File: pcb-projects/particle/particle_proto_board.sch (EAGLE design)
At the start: 38 parts, among them IC1 ATTINY20-MMH, IC2 DMC2400V, IC3 DMC2400V

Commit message: routing board
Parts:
- removed SPI: 332-06, con-garry:332-06
- removed TP10, TP11, TP12, TP13, TP14, TP4, TP5, TP6, TP7, TP8, TP9: TPSPAD1-13, testpad:TPSPAD1-13
- added C1: 100n, rcl:C-EUC0805
- added ISP: 332-06, con-garry:332-06
- added PAD1, PAD4, PAD5: TP1, wirepad:1,6/0,9
- added PAD10: TP10, wirepad:1,6/0,9
- added PAD11: TP11, wirepad:1,6/0,9
- added PAD2: TP2, wirepad:1,6/0,9
- added PAD3: TP3, wirepad:1,6/0,9
- added PAD6: TP6, wirepad:1,6/0,9
- added PAD7: TP7, wirepad:1,6/0,9
- added PAD8: TP8, wirepad:1,6/0,9
- added PAD9: TP9, wirepad:1,6/0,9
- R1, R12, R2: device rcl:R-EU_R1210 -> rcl:R-EU_R0805
- R13, R14, R3, R4, R5, R6, R9: value 470 -> 1k; device rcl:R-EU_R1210 -> rcl:R-EU_R0805
- renumbered RXB1 to RXB, RXB2 to RXA, RXB_LED1 to RXB_LED, RXB_LED2 to RXA_LED, TXB1 to TXB, TXB2 to TXA, TXB_LED1 to TXB_LED, TXB_LED2 to TXA_LED
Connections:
- removed net MISO: IC1B.PB2, LED3.A, SPI-1.S, TP12.PP
- removed net PWR_TX_A: IC1B.PA4, IC2A.G, TP14.PP
- removed net RX_A: IC1B.PA5, IC2B.D, RXA.P, RXA_LED.A, TP4.PP
- removed net TPI_CLK: IC1B.PB0, TPI-3.S
- new net MISO/SW_PWR_RX_A: IC1B.PB2, IC2B.G, ISP-1.S, PAD7.P
- new net TPI_CLK/SW_PWR_RX_A: IC1B.PB0, IC2B.D, PAD6.P, RXA.P, RXA_LED.A, TPI-3.S
- new net TPI_DATA/MOSI/PWR_TX_A: IC1B.PB1, IC2A.G, PAD5.P
- net GND: now also C1.2, ISP-6.S; no longer SPI-6.S
- net N$1: now also PAD8.P; no longer TP7.PP
- net N$2: now also PAD4.P; no longer TP6.PP
- net N$21: now also PAD1.P; no longer TP10.PP
- net PWR_TX_B: now also PAD9.P; no longer TP13.PP
- net RESET: now also ISP-5.S; no longer SPI-5.S
- net RX_B: now also PAD10.P; no longer TP8.PP
- net SCK: now also ISP-3.S, PAD2.P; no longer SPI-3.S, TP11.PP
- net SW_PWR_RX_A: now also IC1B.PA5, LED3.A, PAD3.P; no longer IC1B.PA3, IC2B.G, TP5.PP
- net SW_PWR_RX_B: now also PAD11.P; no longer TP9.PP
- net TPI_DATA/MOSI: now also ISP-4.S; no longer IC1B.PB1, SPI-4.S
- net VCC: now also C1.1, ISP-2.S; no longer SPI-2.S
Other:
- note added: "RX/TX-A"
- note added: "RX/TX-B"
- moved on the sheet: IC1B, LED1, LED2, LED3, R1, R3, R4, R5, RESET-SW, TPI-1, TPI-2, TPI-3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

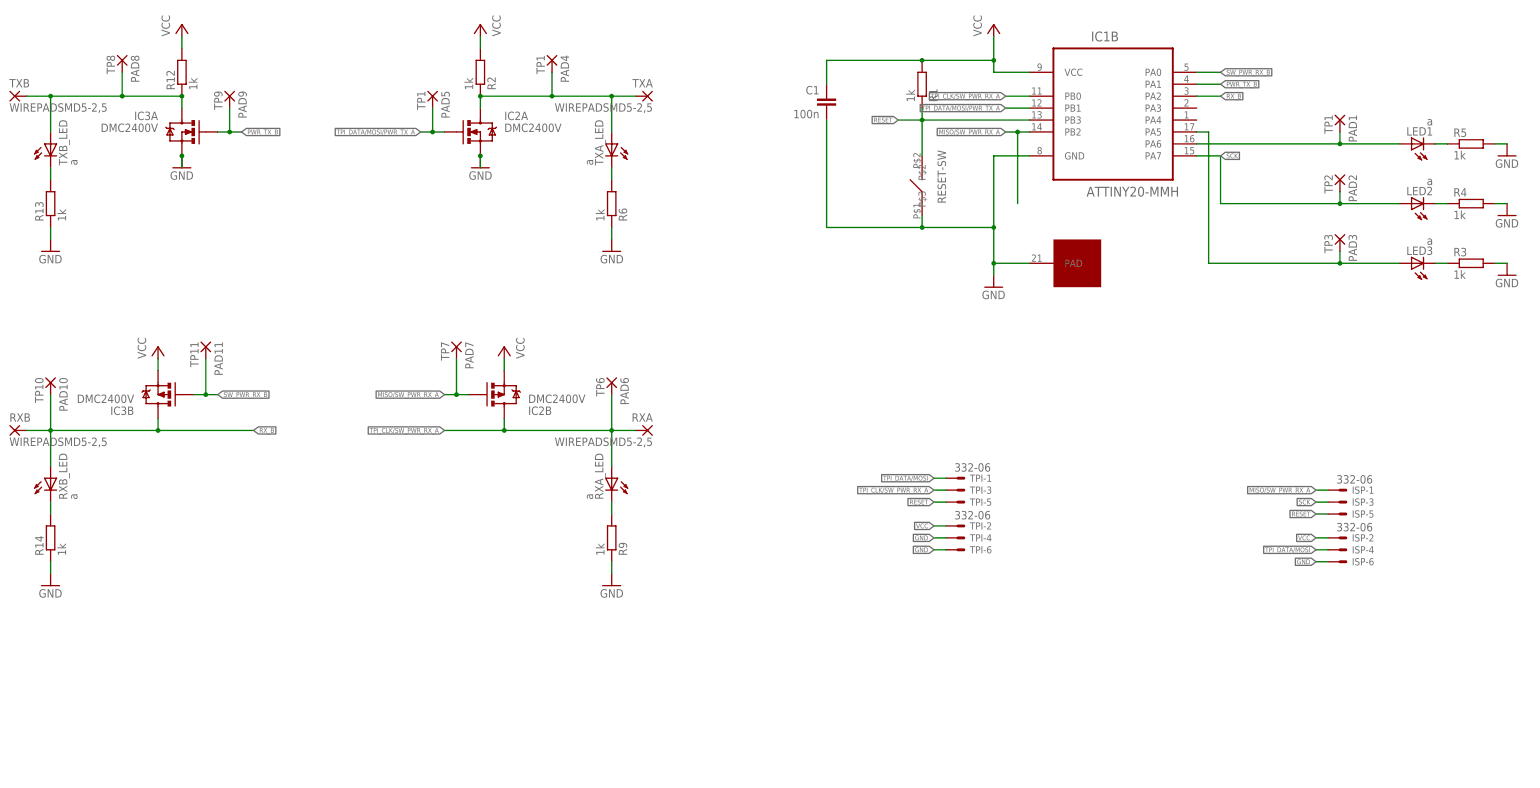
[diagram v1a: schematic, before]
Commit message: close #26, close #31, close #30, close #28, close #25, close #24, close #23
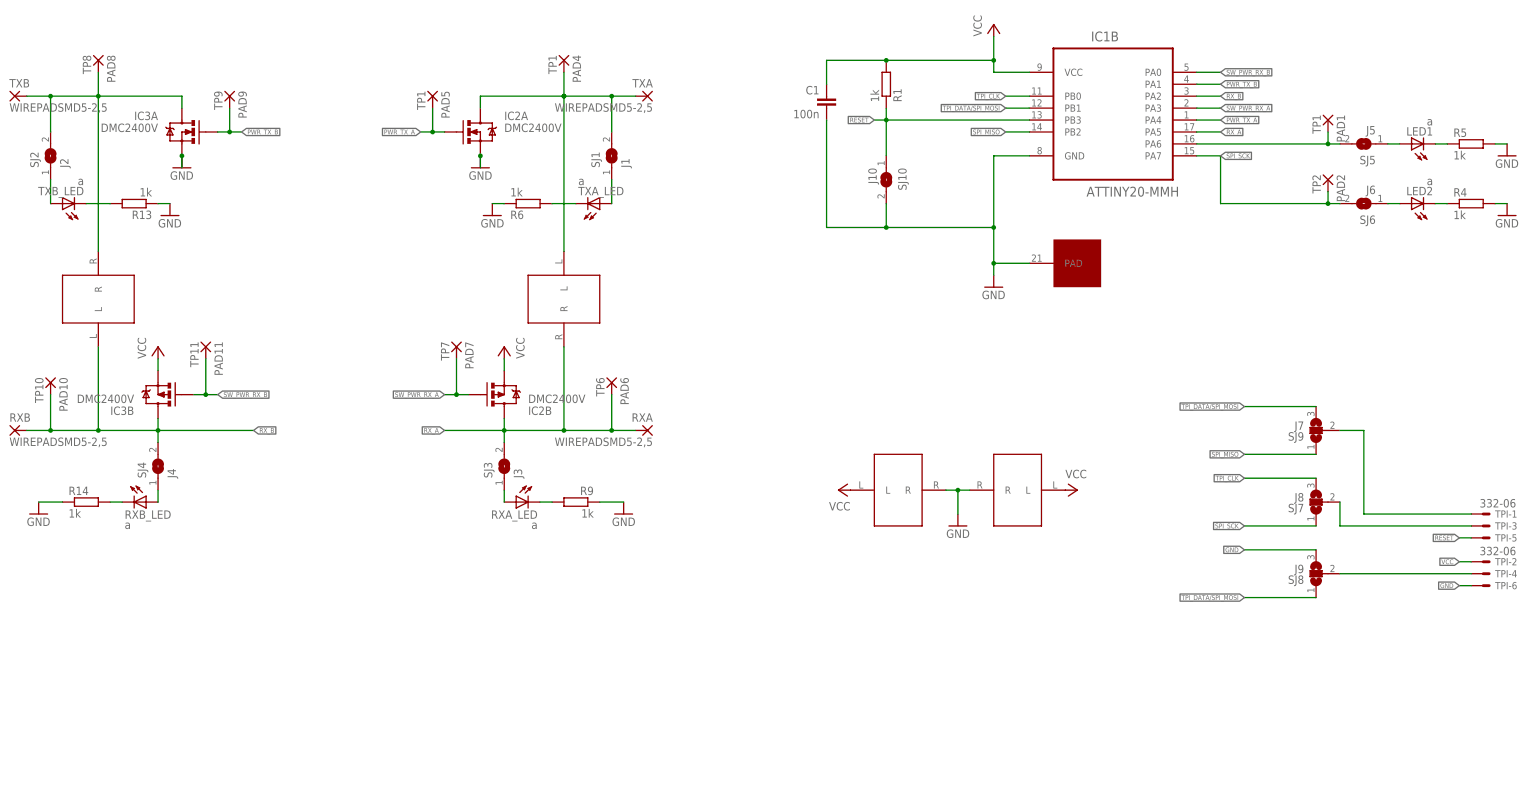
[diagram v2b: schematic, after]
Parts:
- removed ISP: 332-06, con-garry:332-06
- removed LED3: a, led:LEDSML1206
- removed PAD3: TP3, wirepad:1,6/0,9
- removed R12, R2, R3: 1k, rcl:R-EU_R0805
- removed RESET-SW: PAD-RESET-SWITCH, reset_pad:PAD-RESET-SWITCH
- added SJ1: J1, jumper:SJ
- added SJ10: J10, jumper:SJ
- added SJ2: J2, jumper:SJ
- added SJ3: J3, jumper:SJ
- added SJ4: J4, jumper:SJ
- added SJ5: J5, jumper:SJ
- added SJ6: J6, jumper:SJ
- added SJ7: J8, jumper:SJ2W
- added SJ8: J9, jumper:SJ2W
- added SJ9: J7, jumper:SJ2W
- added U$1, U$2, U$3, U$4: SMA-DUAL-CONNSMALL, connectors:SMA-DUAL-CONNSMALL
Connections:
- removed net MISO/SW_PWR_RX_A: IC1B.PB2, IC2B.G, ISP-1.S, PAD7.P
- removed net N$26: LED3.C, R3.1
- removed net SCK: IC1B.PA7, ISP-3.S, LED2.A, PAD2.P
- removed net TPI_CLK/SW_PWR_RX_A: IC1B.PB0, IC2B.D, PAD6.P, RXA.P, RXA_LED.A, TPI-3.S
- removed net TPI_DATA/MOSI: ISP-4.S, TPI-1.S
- removed net TPI_DATA/MOSI/PWR_TX_A: IC1B.PB1, IC2A.G, PAD5.P
- new net N$11: IC1B.PA6, PAD1.P, SJ5.2
- new net N$12: RXA_LED.A, SJ3.1
- new net N$13: SJ2.1, TXB_LED.A
- new net N$14: SJ1.1, TXA_LED.A
- new net N$15: SJ8.2, TPI-4.S
- new net N$17: LED2.A, SJ6.1
- new net N$18: LED1.A, SJ5.1
- new net N$20: SJ7.2, TPI-3.S
- new net N$7: RXB_LED.A, SJ4.1
- new net PWR_TX_A: IC1B.PA4, IC2A.G, PAD5.P
- new net RX_A: IC1B.PA5, IC2B.D, PAD6.P, RXA.P, SJ3.2, U$1.R
- new net SPI_MISO: IC1B.PB2, SJ9.1
- new net SPI_SCK: IC1B.PA7, PAD2.P, SJ6.2, SJ7.1
- new net TPI_CLK: IC1B.PB0, SJ7.3
- new net TPI_DATA/SPI_MOSI: IC1B.PB1, SJ8.1, SJ9.3
- net GND: now also SJ10.2, SJ8.3, U$3.R, U$4.R; no longer ISP-6.S, R3.2, RESET-SW.P$2, TPI-4.S
- net N$1: now also SJ2.2, U$2.R; no longer R12.1, TXB_LED.A
- net N$2: now also SJ1.2, U$1.L; no longer R2.1, TXA_LED.A
- net N$21: now also SJ9.2, TPI-1.S; no longer IC1B.PA6, LED1.A, PAD1.P
- net RESET: now also SJ10.1; no longer ISP-5.S, RESET-SW.P$3
- net RX_B: now also SJ4.2, U$2.L; no longer RXB_LED.A
- net SW_PWR_RX_A: now also IC1B.PA3, IC2B.G, PAD7.P; no longer IC1B.PA5, LED3.A, PAD3.P
- net VCC: now also U$3.L, U$4.L; no longer ISP-2.S, R12.2, R2.2
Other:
- note added: "POWER SUPPLY"
- note added: "TPI/SPI-HEADER"
- moved on the sheet: PAD1, PAD2, PAD4, PAD8, R1, R13, R14, R6, R9, RXA_LED, RXB_LED, TPI-1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

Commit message: close #27, close #19, close #30,skip / close #18, skip / close #14
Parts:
- removed PAD10: TP10, wirepad:1,6/0,9
- removed PAD11: TP11, wirepad:1,6/0,9
- removed PAD4, PAD5: TP1, wirepad:1,6/0,9
- removed PAD6: TP6, wirepad:1,6/0,9
- removed PAD7: TP7, wirepad:1,6/0,9
- removed PAD8: TP8, wirepad:1,6/0,9
- removed PAD9: TP9, wirepad:1,6/0,9
- removed SJ1: J1, jumper:SJ
- removed SJ2: J2, jumper:SJ
- removed SJ3: J3, jumper:SJ
- removed SJ4: J4, jumper:SJ
- removed SJ7: J8, jumper:SJ2W
- removed SJ8: J9, jumper:SJ2W
- removed SJ9: J7, jumper:SJ2W
- removed TPI: 332-06, con-garry:332-06
- removed U$1, U$2, U$3, U$4: SMA-DUAL-CONNSMALL, connectors:SMA-DUAL-CONNSMALL
- added GND_B: GND_B, wirepad:1,6/0,9
- added GND_T: GND_T, wirepad:1,6/0,9
- added PI: 332-06, con-garry:332-06
- added PWR_TX_A: PWR_TX_A, wirepad:1,6/0,9
- added PWR_TX_B: PWR_TX_B, wirepad:1,6/0,9
- added SW1: SW1, jumper:SJ2W
- added SW2: SW2, jumper:SJ2W
- added SW3: SW3, jumper:SJ2W
- added SWLED3: J2, jumper:SJ
- added SWLED4: J4, jumper:SJ
- added SWLED5: J1, jumper:SJ
- added SWLED6: J3, jumper:SJ
- added SW_PWR_RX_A: SW_PWR_RX_A, wirepad:1,6/0,9
- added SW_PWR_RX_B: SW_PWR_RX_B, wirepad:1,6/0,9
- added TPRXA: TPRXA, wirepad:1,6/0,9
- added TPRXB: TPRXB, wirepad:1,6/0,9
- added TPTXA: TPTXA, wirepad:1,6/0,9
- added TPTXB: TPTXB, wirepad:1,6/0,9
- added VCC_B: VCC_B, wirepad:1,6/0,9
- added VCC_T: VCC_T, wirepad:1,6/0,9
- LED1, LED2, RXA_LED, RXB_LED, TXA_LED, TXB_LED: value a -> x
- RESET: value J10 -> RESET
- RXA: value WIREPADSMD5-2,5 -> RXA; device wirepad:WIREPADSMD5-2,5 -> wirepad:1,6/0,9
- RXB: value WIREPADSMD5-2,5 -> RXB; device wirepad:WIREPADSMD5-2,5 -> wirepad:1,6/0,9
- TXA: value WIREPADSMD5-2,5 -> TXA; device wirepad:WIREPADSMD5-2,5 -> wirepad:1,6/0,9
- TXB: value WIREPADSMD5-2,5 -> TXB; device wirepad:WIREPADSMD5-2,5 -> wirepad:1,6/0,9
- renumbered PAD1 to TP1, PAD2 to TP2, SJ10 to RESET, SJ5 to SWLED1, SJ6 to SWLED2
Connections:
- removed net N$1: IC3A.D, PAD8.P, SJ2.2, TXB.P, U$2.R
- removed net N$2: IC2A.D, PAD4.P, SJ1.2, TXA.P, U$1.L
- new net TX_A: IC2A.D, SWLED5.2, TPTXA.P, TXA.P
- new net TX_B: IC3A.D, SWLED3.2, TPTXB.P, TXB.P
- net GND: now also GND_B.P, GND_T.P, PI-6.S, SW3.3; no longer SJ8.3, TPI-6.S, U$3.R, U$4.R
- net N$12: now also SWLED6.1; no longer SJ3.1
- net N$13: now also SWLED3.1; no longer SJ2.1
- net N$14: now also SWLED5.1; no longer SJ1.1
- net N$15: now also PI-4.S, SW3.2; no longer SJ8.2, TPI-4.S
- net N$20: now also PI-3.S, SW2.2; no longer SJ7.2, TPI-3.S
- net N$21: now also PI-1.S, SW1.2; no longer SJ9.2, TPI-1.S
- net N$7: now also SWLED4.1; no longer SJ4.1
- net PWR_TX_A: now also PWR_TX_A.P; no longer PAD5.P
- net PWR_TX_B: now also IC1B.PA0, PWR_TX_B.P; no longer IC1B.PA1, PAD9.P
- net RESET: now also PI-5.S; no longer TPI-5.S
- net RX_A: now also SWLED6.2, TPRXA.P; no longer PAD6.P, SJ3.2, U$1.R
- net RX_B: now also SWLED4.2, TPRXB.P; no longer PAD10.P, SJ4.2, U$2.L
- net SPI_MISO: now also SW1.1; no longer SJ9.1
- net SPI_SCK: now also SW2.1; no longer SJ7.1
- net SW_PWR_RX_A: now also SW_PWR_RX_A.P; no longer PAD7.P
- net SW_PWR_RX_B: now also IC1B.PA1, SW_PWR_RX_B.P; no longer IC1B.PA0, PAD11.P
- net TPI_CLK: now also SW2.3; no longer SJ7.3
- net TPI_DATA/SPI_MOSI: now also SW1.3, SW3.1; no longer SJ8.1, SJ9.3
- net VCC: now also PI-2.S, VCC_B.P, VCC_T.P; no longer TPI-2.S, U$3.L, U$4.L
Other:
- note added: "TPI/SPI-CONNECTOR"
- note added: "| SPI | TPI -------------- SW1 | 2-3 | 1-2 SW2 | 2-3 | 1-2 SW3 | 2-3 | 1-2"
- note removed: "TPI/SPI-HEADER"
- moved on the sheet: C1, IC2A, IC2B, IC3A, IC3B, R13, R14, R6, R9, RXA_LED, RXB_LED, TXA_LED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

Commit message: routed isp header
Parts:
- added R2, R3, R7, R8: 0, rcl:R-EU_R2010
- PWR/TX_A: value PWR_TX_A -> PWR/TX_A
- PWR/TX_B: value PWR_TX_B -> PWR/TX_B
- R1, R13, R14, R4, R5, R6, R9: device rcl:R-EU_R0805 -> rcl:R-EU_R2010
- renumbered PWR_TX_A to PWR/TX_A, PWR_TX_B to PWR/TX_B
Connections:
- net PWR_TX_A renamed PWR/TX_A
- net PWR_TX_B renamed PWR/TX_B
- net SW_PWR_RX_A renamed SW_PWR/RX_A
- net SW_PWR_RX_B renamed SW_PWR/RX_B
- new net N$1: R3.1, SW1.2
- new net N$16: R8.1, SW3.2
- new net N$19: PI-4.S, R8.2
- new net N$2: IC1B.PB3, R2.1
- net N$15: now also PI-3.S, R7.1; no longer PI-4.S, SW3.2
- net N$20: now also R7.2; no longer PI-3.S
- net N$21: now also R3.2; no longer SW1.2
- net RESET: now also R2.2; no longer IC1B.PB3
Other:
- moved on the sheet: C1, PI-1, PI-2, PI-3, PI-4, PI-5, PI-6, R1, RESET, SW1, SW2, SW3

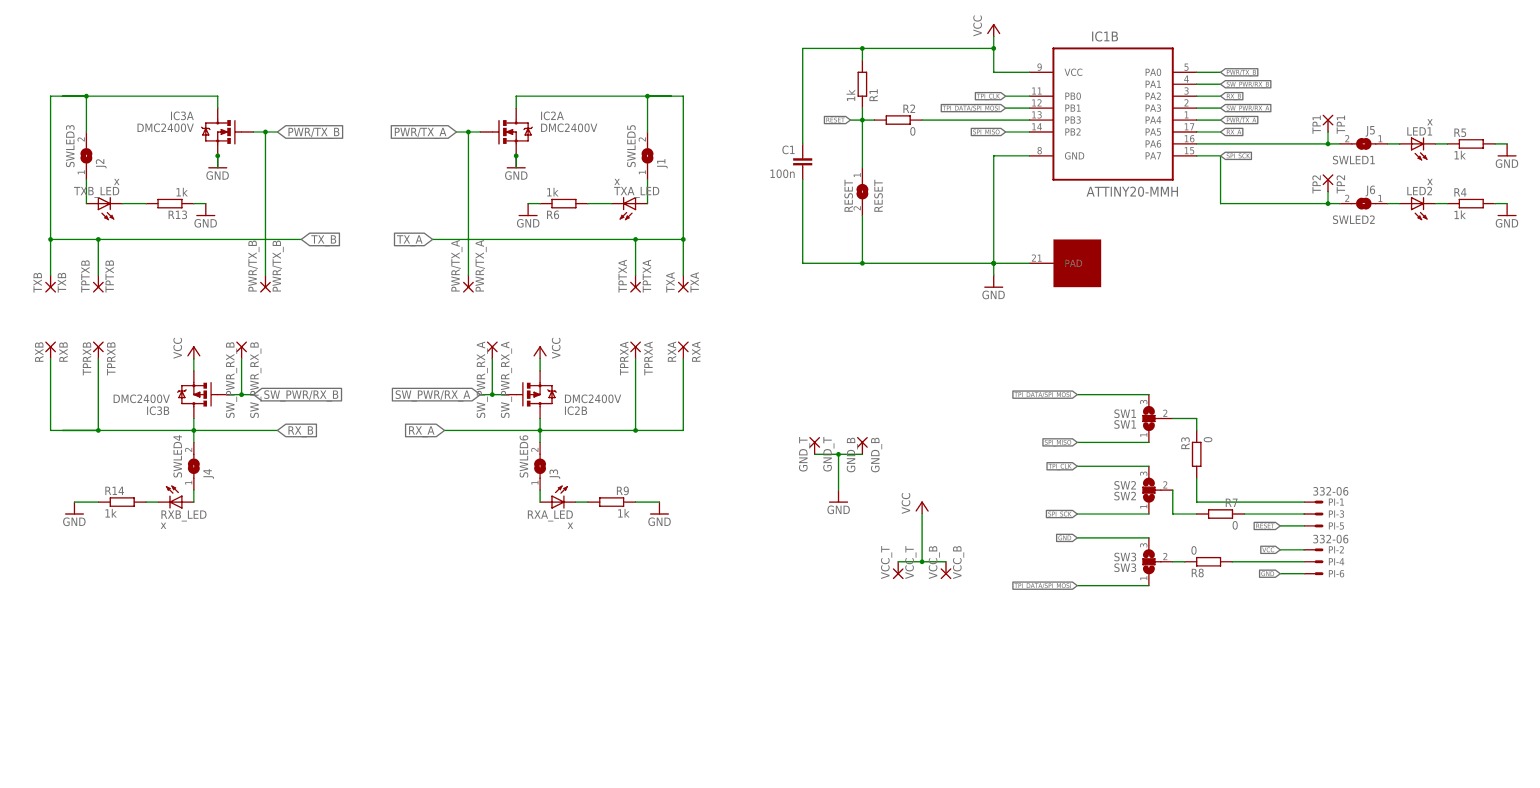
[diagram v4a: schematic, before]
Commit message: routed board - usable version without filling in gnd/vcc fields
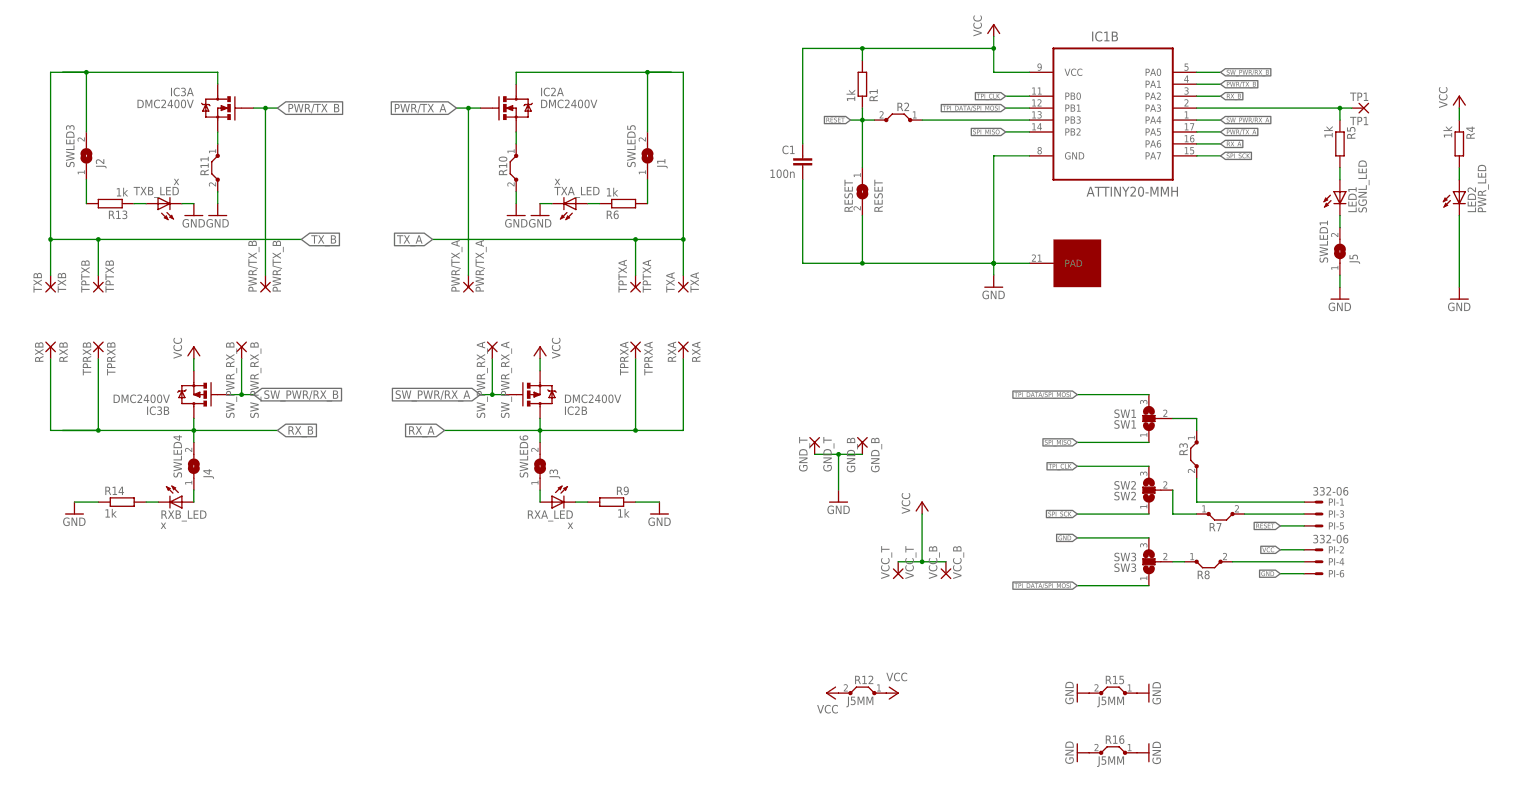
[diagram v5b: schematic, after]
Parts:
- removed SWLED2: J6, jumper:SJ
- removed TP2: TP2, wirepad:1,6/0,9
- added R10, R11, R12, R15, R16: J5MM, jumper:J5MM
- C1: device rcl:C-EUC0805 -> rcl:C-EUC1206
- LED1: value x -> SGNL_LED
- LED2: value x -> PWR_LED
- R2, R3, R7, R8: value 0 -> J5MM; device rcl:R-EU_R2010 -> jumper:J5MM
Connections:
- removed net N$25: LED2.C, R4.1
- new net N$22: LED2.A, R4.2
- new net N$23: LED1.C, SWLED1.2
- net GND: now also LED2.C, R10.2, R11.2, R15.1, R15.2, R16.1, R16.2, SWLED1.1, TXA_LED.C, TXB_LED.C; no longer IC2A.S, IC3A.S, R13.1, R4.2, R5.2, R6.1
- net N$11: now also IC1B.PA3, R5.1; no longer IC1B.PA6, SWLED1.2
- net N$13: now also R13.1; no longer SWLED3.1
- net N$14: now also R6.2; no longer TXA_LED.A
- net N$15: now also R7.2; no longer R7.1
- net N$17: now also IC3A.S, R11.1; no longer LED2.A, SWLED2.1
- net N$18: now also R5.2; no longer SWLED1.1
- net N$20: now also R7.1; no longer R7.2
- net N$24: now also IC2A.S, R10.1; no longer LED1.C, R5.1
- net N$3: now also R6.1, TXA_LED.A; no longer R6.2, TXA_LED.C
- net N$6: now also SWLED3.1; no longer TXB_LED.C
- net PWR/TX_A: now also IC1B.PA5; no longer IC1B.PA4
- net PWR/TX_B: now also IC1B.PA1; no longer IC1B.PA0
- net RX_A: now also IC1B.PA6; no longer IC1B.PA5
- net SPI_SCK: no longer SWLED2.2, TP2.P
- net SW_PWR/RX_A: now also IC1B.PA4; no longer IC1B.PA3
- net SW_PWR/RX_B: now also IC1B.PA0; no longer IC1B.PA1
- net VCC: now also R12.1, R12.2, R4.1
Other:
- moved on the sheet: IC2A, IC3A, LED1, LED2, R13, R4, R5, R6, SWLED1, TP1, TXA_LED, TXB_LED
